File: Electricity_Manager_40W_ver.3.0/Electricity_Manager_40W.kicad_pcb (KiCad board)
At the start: 2 copper layers, 100 x 77 mm, 198 parts, among them IC2 MAIN_SHUTDOWN, IC3 RELAY_STATE, IC4 ADC_RST, J1 SERIAL, P1 SWD, P10 EMERGENCY, P11 EMERGENCY, P12 FRAME_GRAND, P13 BATT_IN, P15 OUT_B, P16 BATT_IN, P17 OUT_A, P2 CAN, P3 CAN, P4 EMERGENCY_SIGNAL, P5 EMERGENCY_SIGNAL, P6 12V_OUT, P7 12V_OUT, P8 MAIN_~RST, P9 MAIN_SW, Q1 FET_N, Q2 NPN, Q3 NPN, Q4 FET_N, Q7 FET_N, SW1 RST, SW2 SW0, SW3 SW1, U1 MAX3051, U10 BD9G101G, U11 OUTA_CHECK, U12 LOGO, U13 LOGO, U14 OUTB_CHECK, U15 BD33FA1, U16 LOGO, U17 LOGO, U18 LOGO, U19 MCP2221A, U2 STM32F405RG, U20 OSRB38C9AA, U21 OSRB38C9AA, U22 HSIN_946, U23 LOGO, U25 LOGO, U3 FULL COLOR, U4 AQM0802_BL, U5 AP3211, U6 SI8900, U7 AZ1086H, U8 ACS70331, U9 LOGO, X1 8MHz

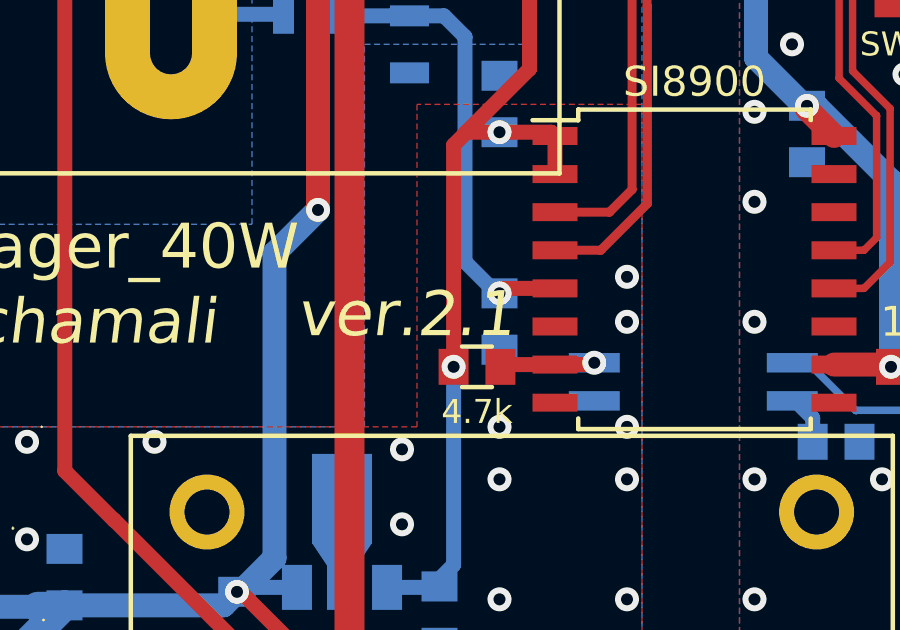
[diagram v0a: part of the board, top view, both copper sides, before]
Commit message: 電源基板のシルク表記を直しただけ
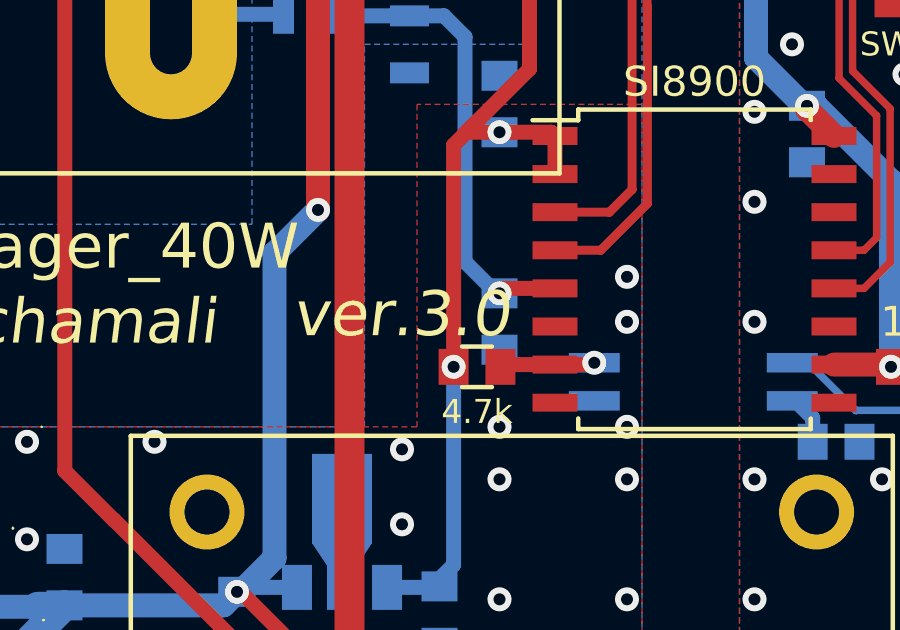
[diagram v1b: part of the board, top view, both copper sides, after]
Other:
- board text added: "ver.3.0"
- board text removed: "ver.2.1"
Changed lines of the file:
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@@
       (drillshape 0)
       (scaleselection 1)
-      (outputdirectory "C:/Users/3Zuta/Documents/NHK_RC20_PCBs/Electricity_Manager_40W_ver.2.1/加工/"))
+      (outputdirectory "C:/Users/3Zuta/Documents/NHK_RC20_PCBs/Electricity_Manager_40W_ver.3.0/加工/"))
   )
   (net 0 "")
@@
     )
   )
-  (gr_text ver.2.1 (at 94.75 145.5) (layer F.SilkS)
+  (gr_text ver.3.0 (at 94.6 145.5) (layer F.SilkS)
     (effects (font (size 1.5 1.5) (thickness 0.375) italic) (justify left))
   )
